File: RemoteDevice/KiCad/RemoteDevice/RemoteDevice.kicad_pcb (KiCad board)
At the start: 2 copper layers, 98 x 52 mm, 56 parts, among them J1 pin, J2 pin, Q1 PJA3411, Q2 PJA3411, SW1 BP, SW2 BP, U1 XC9140, U10 XBEE-3, U2 STM32L041F6Px, U3 MCP6281, U4 ADT7410TRZ, U5 MCP6281, U6 RT606, U7 Microphone, U8 LD2981CU33, U9 Con_4pts

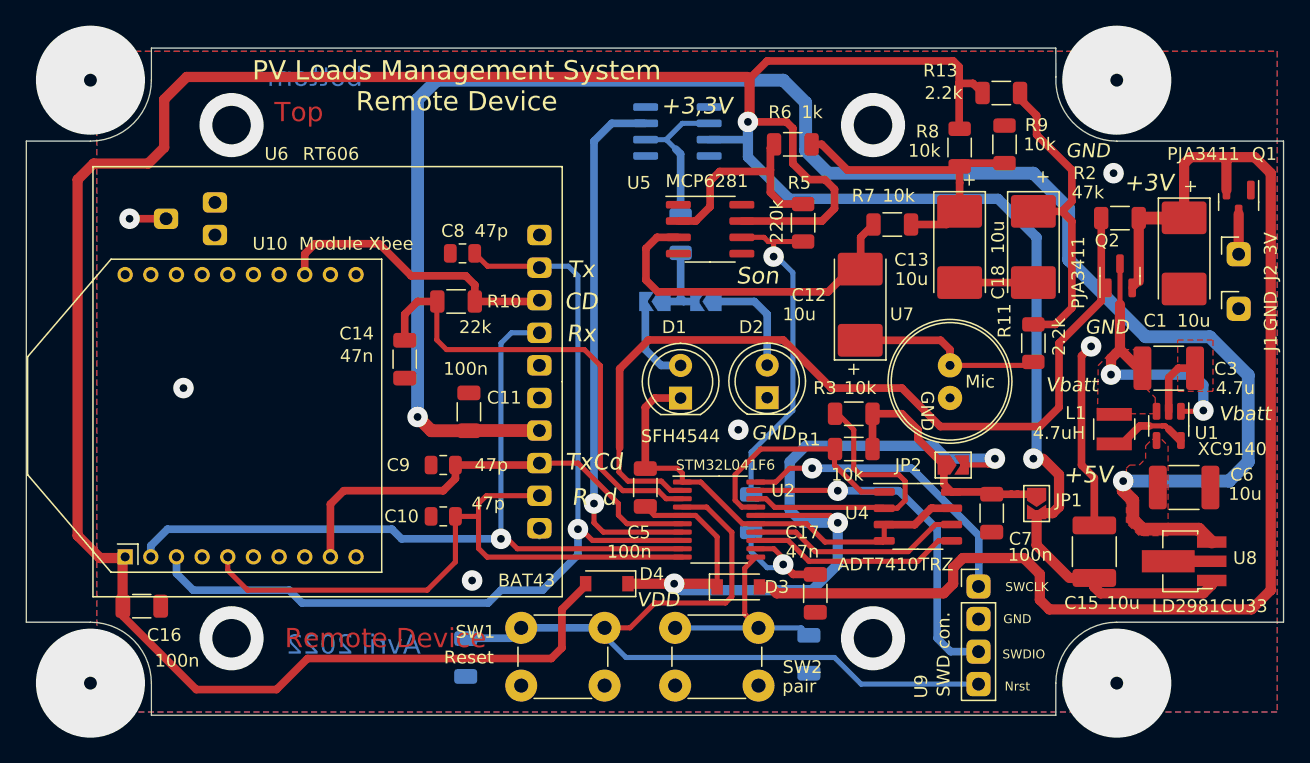
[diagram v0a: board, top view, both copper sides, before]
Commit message: refonte du répertoire. Révision complète SySML pour y inclure la notion de Gateway et de SystemManager (Raspberry pi et touch screen). Revoir le protocole RDG en profondeur selon SysML à faire en premier
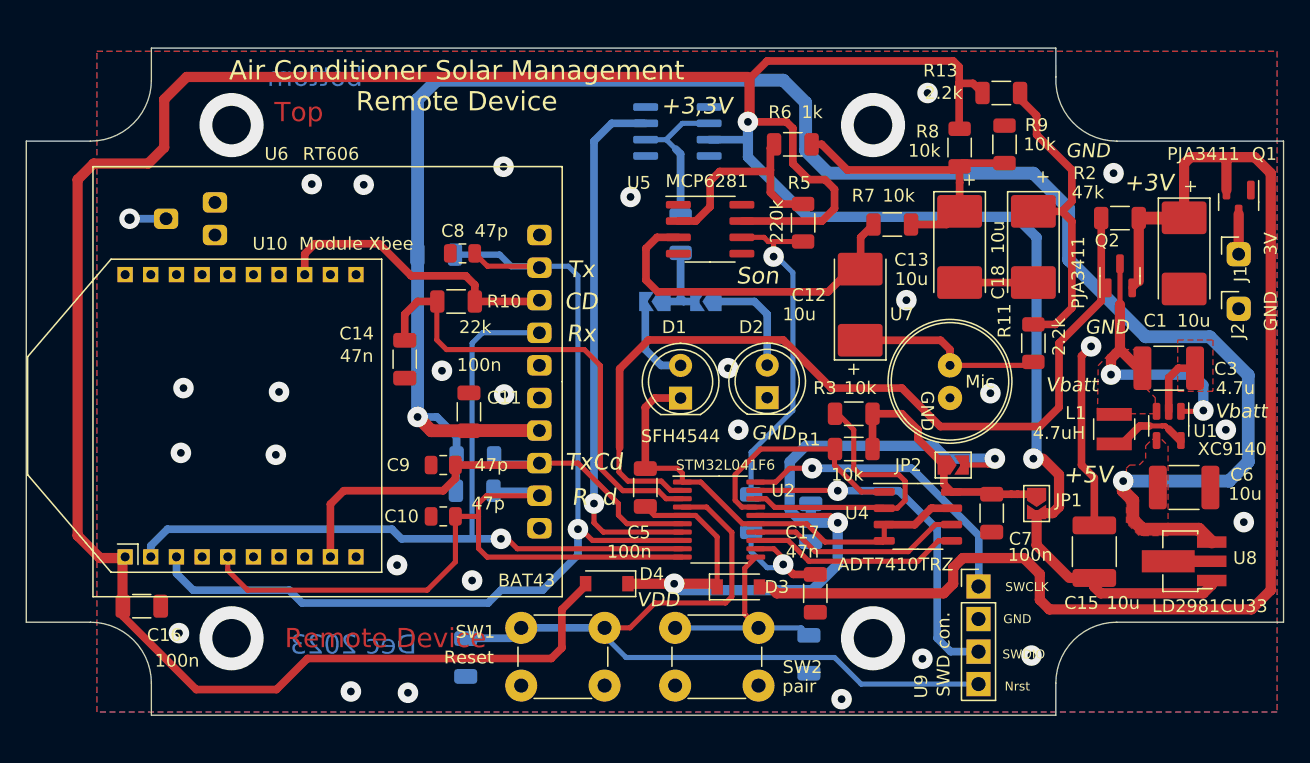
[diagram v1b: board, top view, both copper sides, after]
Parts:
- added C19: 100n, Capacitor_SMD:C_1206_3216Metric, B.Cu at (84.2, 100.0)
- added R14: 10k, Resistor_SMD:R_1206_3216Metric, B.Cu at (55.0, 79.1)
- added R15: 10k, Resistor_SMD:R_1206_3216Metric, B.Cu at (58.0, 94.9)
- added R16: 10k, Resistor_SMD:R_1206_3216Metric, B.Cu at (58.0, 97.5)
- C14, C17: value 10n -> 47n
- R10: value 100k -> 22k
- R12: value 4.7k -> 1k
- R4: value 47 -> 150
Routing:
- net +5V: track 141.5 -> 149.4 mm
- net /DataIn: track 74.2 -> 81.2 mm
- net /RxCmde: track 50.4 -> 54.1 mm
- net /TxCmde: track 36.0 -> 39.7 mm
- net /DataOut: track 62.0 -> 64.3 mm
- net VDD: track 68.3 -> 69.7 mm
- net GND: track 62.5 -> 61.6 mm, vias 5 -> 27
- net (no net): vias 8 -> 4
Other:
- board text added: "Air Conditioner Solar Management Remote Device"
- board text added: "Dec 2023"
- board text removed: "Avril 2022"
- board text removed: "PV Loads Management System Remote Device"
